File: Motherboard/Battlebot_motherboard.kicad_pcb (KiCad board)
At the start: 2 copper layers, 42 x 61.5 mm, 52 parts, among them J1 Reciever, J2 12Vin, J3 Fan connector, J4 BEC, J5 Conn_01x02_Socket, J6 Conn_01x02_Socket, U1 XIAO-RP2040-SMD, U2 L9958SBTR, U3 L9958SBTR

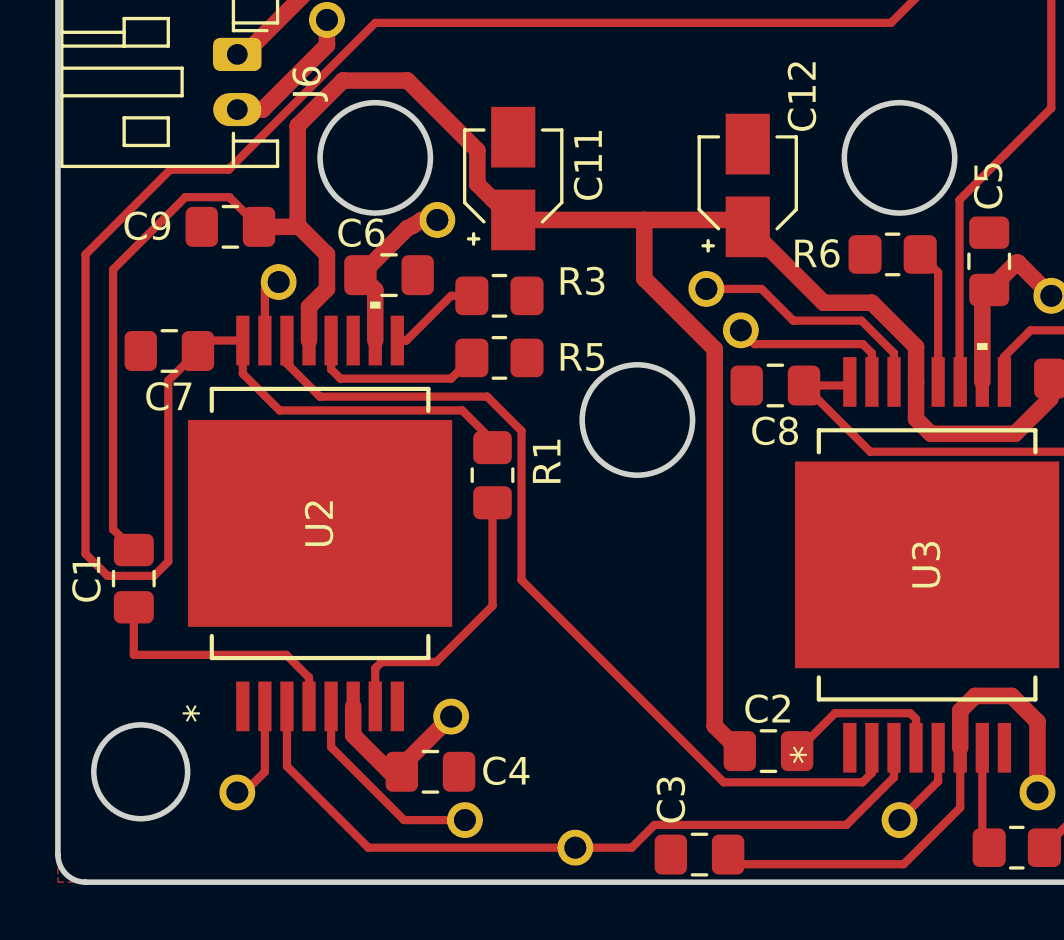
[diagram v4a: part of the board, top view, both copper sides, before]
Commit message: connected more of the ground pours
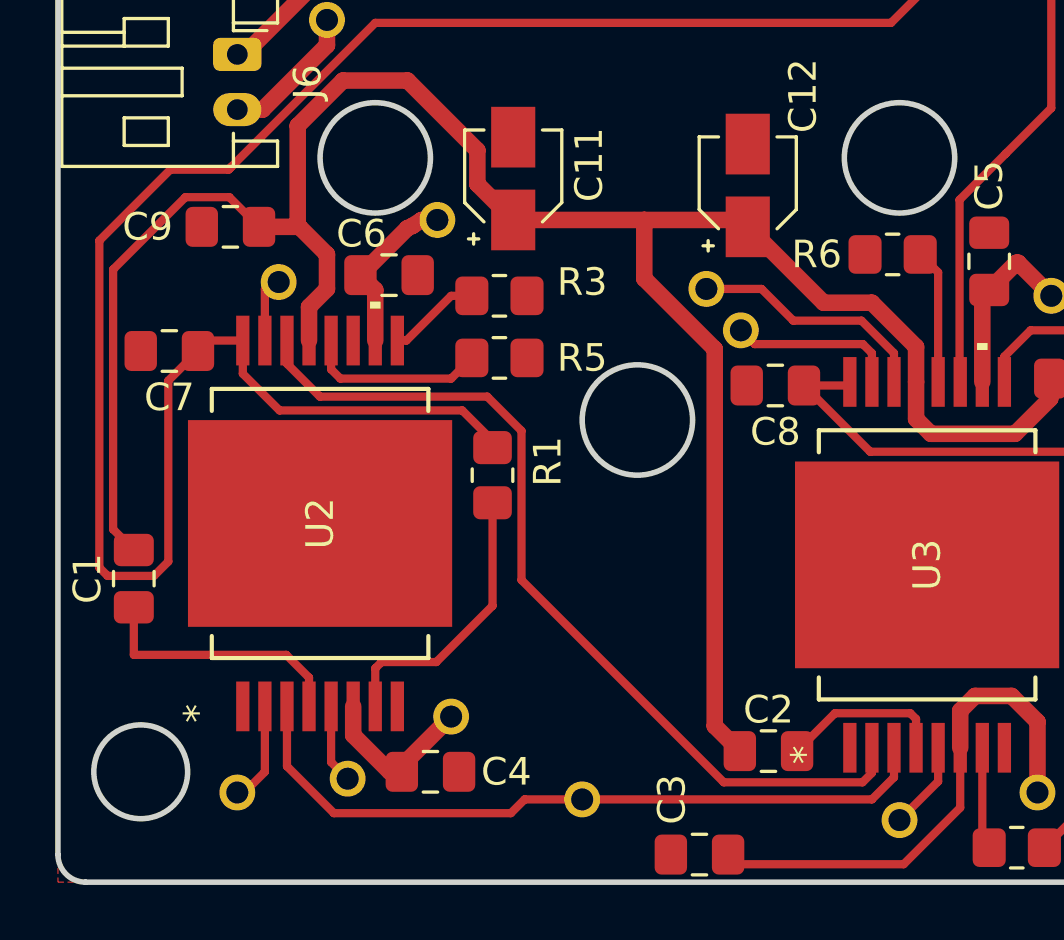
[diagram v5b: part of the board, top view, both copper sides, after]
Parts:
- moved ? 4.51 mm to (158.5, 99.2)
- moved ? 1.77 mm to (167.0, 100.0)
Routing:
- net DIR2: track 32.1 -> 27.5 mm
- net CS: track 31.2 -> 30.2 mm
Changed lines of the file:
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@@
 	(footprint ""
 		(layer "F.Cu")
-		(at 162.75 100.75)
+		(at 158.5 99.25)
 		(property "Reference" ""
 			(at 0 0 0)
@@
 	(footprint ""
 		(layer "F.Cu")
-		(at 166.75 101.75)
+		(at 167 100)
 		(property "Reference" ""
 			(at 0 0 0)
@@
 	)
 	(segment
-		(start 149 80.25)
-		(end 152.071315 77.178685)
-		(width 0.3)
-		(layer "F.Cu")
-		(net 8)
-	)
-	(segment
-		(start 152 91.380456)
-		(end 151.480456 91.9)
-		(width 0.3)
-		(layer "F.Cu")
-		(net 8)
-	)
-	(segment
 		(start 156.03085 85.9035)
 		(end 154.69965 84.5723)
@@
 	)
 	(segment
+		(start 149.5 91.6)
+		(end 149.5 79.75)
+		(width 0.3)
+		(layer "F.Cu")
+		(net 8)
+	)
+	(segment
+		(start 149.5 79.75)
+		(end 152.071315 77.178685)
+		(width 0.3)
+		(layer "F.Cu")
+		(net 8)
+	)
+	(segment
+		(start 153.075 83.75)
+		(end 152 84.825)
+		(width 0.3)
+		(layer "F.Cu")
+		(net 8)
+	)
+	(segment
 		(start 156.797 54.703)
 		(end 156.25 55.25)
@@
 	)
 	(segment
-		(start 184.6379 87.4035)
-		(end 184.6379 88)
+		(start 152 91.380456)
+		(end 151.480456 91.9)
 		(width 0.3)
 		(layer "F.Cu")
@@
 	)
 	(segment
-		(start 154.69965 83.3706)
-		(end 153.4544 83.3706)
+		(start 184.6379 87.4035)
+		(end 184.6379 88)
 		(width 0.3)
 		(layer "F.Cu")
@@
 	)
 	(segment
-		(start 152.071315 77.178685)
-		(end 154.178685 77.178685)
+		(start 154.69965 83.3706)
+		(end 153.4544 83.3706)
 		(width 0.3)
 		(layer "F.Cu")
@@
 	)
 	(segment
-		(start 151.480456 91.9)
-		(end 149.8 91.9)
-		(width 0.3)
-		(layer "F.Cu")
-		(net 8)
-	)
-	(segment
 		(start 154.69965 84.5723)
 		(end 154.69965 83.3706)
@@
 	)
 	(segment
-		(start 156.75 43)
-		(end 156.75 44.96)
+		(start 151.480456 91.9)
+		(end 149.8 91.9)
 		(width 0.3)
 		(layer "F.Cu")
@@
 	)
 	(segment
-		(start 189.35 83.2879)
-		(end 189.35 45.6)
+		(start 149.8 91.9)
+		(end 149.5 91.6)
 		(width 0.3)
 		(layer "F.Cu")
@@
 	)
 	(segment
-		(start 154.178685 77.178685)
-		(end 159.5 71.857371)
+		(start 156.75 43)
+		(end 156.75 44.96)
 		(width 0.3)
 		(layer "F.Cu")
@@
 	)
 	(segment
-		(start 153.075 83.75)
-		(end 152 84.825)
+		(start 189.35 83.2879)
+		(end 189.35 45.6)
 		(width 0.3)
 		(layer "F.Cu")
@@
 	)
 	(segment
-		(start 184.6379 88)
-		(end 184.6379 100.8621)
+		(start 154.178685 77.178685)
+		(end 159.5 71.857371)
 		(width 0.3)
 		(layer "F.Cu")
@@
 	)
 	(segment
-		(start 156.75 44.96)
-		(end 158.5 46.71)
+		(start 184.6379 88)
+		(end 184.6379 100.8621)
 		(width 0.3)
 		(layer "F.Cu")
@@
 	)
 	(segment
-		(start 149 91.1)
-		(end 149 80.25)
+		(start 156.75 44.96)
+		(end 158.5 46.71)
 		(width 0.3)
 		(layer "F.Cu")
@@
 	)
 	(segment
-		(start 178.192629 71.857371)
-		(end 182.05 68)
+		(start 152.071315 77.178685)
+		(end 154.178685 77.178685)
 		(width 0.3)
 		(layer "F.Cu")
@@
 	)
 	(segment
-		(start 157 42.75)
-		(end 156.75 43)
+		(start 152 84.825)
+		(end 152 91.380456)
 		(width 0.3)
 		(layer "F.Cu")
@@
 	)
 	(segment
-		(start 152 84.825)
-		(end 152 91.380456)
+		(start 178.192629 71.857371)
+		(end 182.05 68)
 		(width 0.3)
 		(layer "F.Cu")
@@
 	)
 	(segment
-		(start 149.8 91.9)
-		(end 149 91.1)
+		(start 157 42.75)
+		(end 156.75 43)
 		(width 0.3)
 		(layer "F.Cu")
@@
 	)
 	(segment
+		(start 157.90005 98.65005)
+		(end 158.5 99.25)
+		(width 0.3)
+		(layer "F.Cu")
+		(net 17)
+	)
+	(segment
 		(start 166.4756 46.301)
 		(end 166.4756 47.676)
@@
 	(segment
 		(start 157.90005 96.6294)
-		(end 157.90005 98.105506)
-		(width 0.3)
-		(layer "F.Cu")
-		(net 17)
-	)
-	(segment
-		(start 160.544544 100.75)
-		(end 162.75 100.75)
-		(width 0.3)
-		(layer "F.Cu")
-		(net 17)
-	)
-	(segment
-		(start 157.90005 98.105506)
-		(end 160.544544 100.75)
+		(end 157.90005 98.65005)
 		(width 0.3)
 		(layer "F.Cu")
@@
 	)
 	(segment
-		(start 168.794544 101.75)
-		(end 169.619544 100.925)
+		(start 164.914214 100)
+		(end 177.5 100)
 		(width 0.3)
 		(layer "F.Cu")
@@
 	)
 	(segment
-		(start 178.29985 99.20015)
-		(end 178.29985 98.1294)
+		(start 164.414214 100.5)
+		(end 164.914214 100)
 		(width 0.3)
 		(layer "F.Cu")
@@
 	)
 	(segment
-		(start 159.25 101.75)
-		(end 168.794544 101.75)
+		(start 156.29985 96.6294)
+		(end 156.29985 98.79985)
 		(width 0.3)
 		(layer "F.Cu")
@@
 	)
 	(segment
-		(start 163.9356 64.8144)
-		(end 163 65.75)
+		(start 178.29985 99.20015)
+		(end 178.29985 98.1294)
 		(width 0.3)
 		(layer "F.Cu")
@@
 	)
 	(segment
-		(start 176.575 100.925)
-		(end 178.29985 99.20015)
+		(start 163.9356 64.8144)
+		(end 163 65.75)
 		(width 0.3)
 		(layer "F.Cu")
@@
 	)
 	(segment
-		(start 156.29985 96.6294)
-		(end 156.29985 98.79985)
+		(start 156.29985 98.79985)
+		(end 158 100.5)
 		(width 0.3)
 		(layer "F.Cu")
@@
 	)
 	(segment
-		(start 169.619544 100.925)
-		(end 176.575 100.925)
+		(start 158 100.5)
+		(end 164.414214 100.5)
 		(width 0.3)
 		(layer "F.Cu")
@@
 	)
 	(segment
-		(start 156.29985 98.79985)
-		(end 159.25 101.75)
+		(start 163.9356 62.466)
+		(end 163.9356 64.8144)
 		(width 0.3)
 		(layer "F.Cu")
@@
 	)
 	(segment
-		(start 163.9356 62.466)
-		(end 163.9356 64.8144)
+		(start 177.5 100)
+		(end 178.29985 99.20015)
 		(width 0.3)
 		(layer "F.Cu")

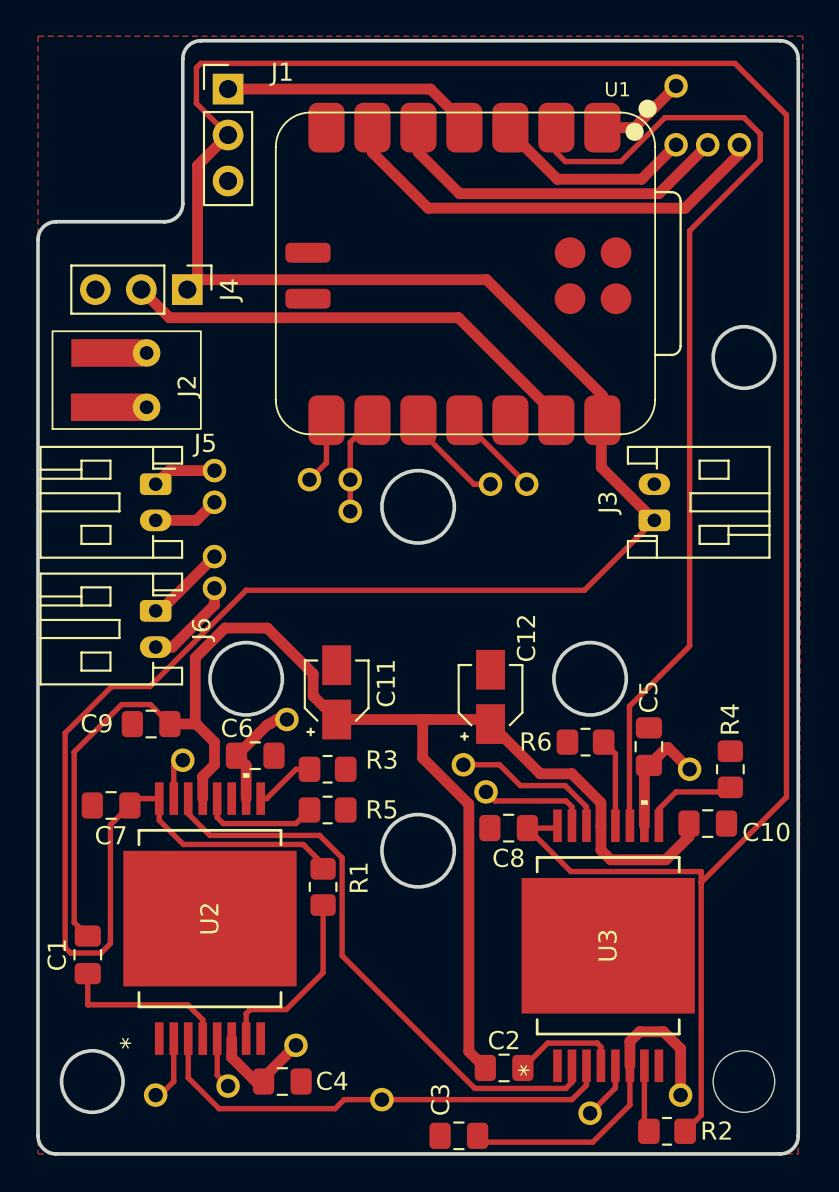
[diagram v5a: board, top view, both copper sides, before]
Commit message: reroute using 2 layers and fix 1 connector
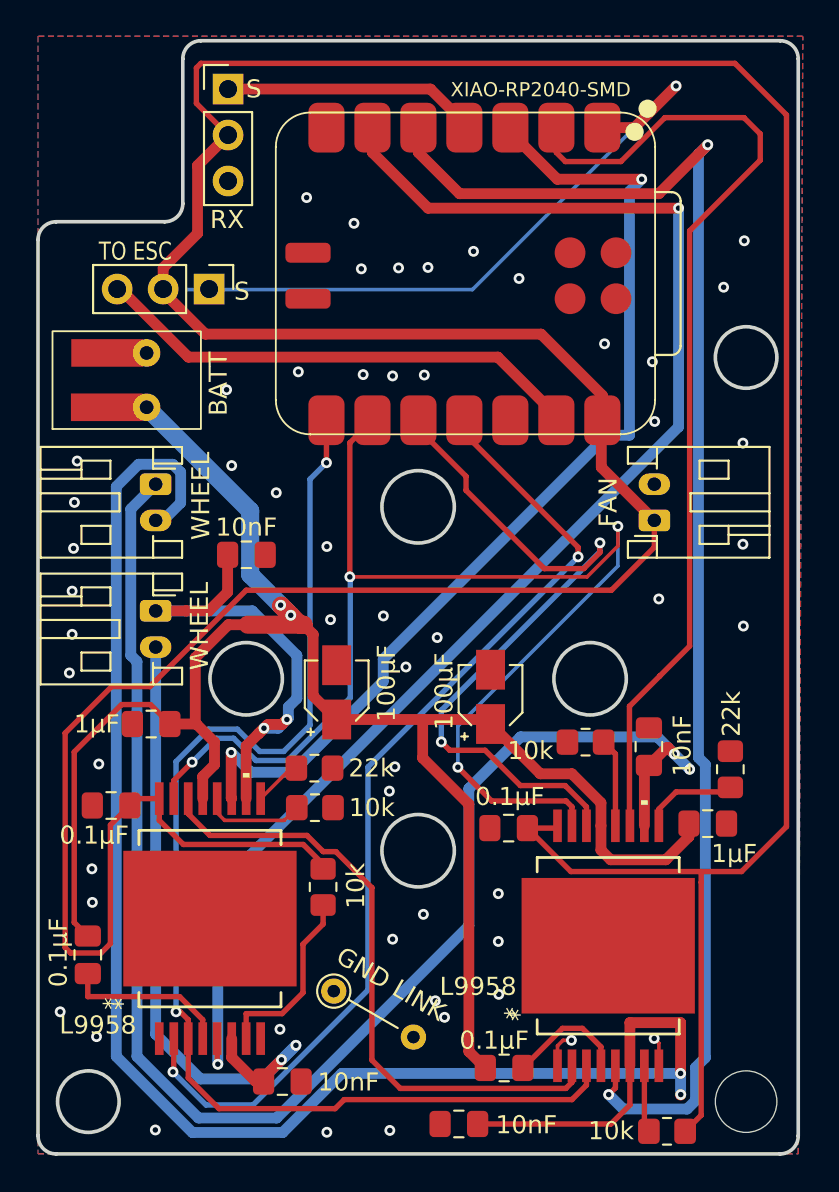
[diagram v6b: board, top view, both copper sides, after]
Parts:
- removed ? (x23): , 
- removed the REF** at (186.8, 47.2)
- added GND LINK: 0, Resistor_THT:R_Axial_DIN0204_L3.6mm_D1.6mm_P5.08mm_Vertical, F.Cu at (164.3, 94.0)
- TO ESC: renamed from J4
- moved 10nF 11.1 mm to (159.5, 69.9)
- moved TO ESC 1.20 mm to (157.5, 55.2)
- moved 22k 0.73 mm to (163.3, 81.7)
- moved 10k 0.72 mm to (163.3, 83.9)
- moved 10nF 0.65 mm to (171.2, 101.3)
- renumbered C2 to 0.1µF, C7 to 0.1µF, C8 to 0.1µF, C1 to 0.1µF, C11 to 100µF, C12 to 100µF, R5 to 10k, R1 to 10k, R6 to 10k, R2 to 10k, C4 to 10nF, C5 to 10nF, C6 to 10nF, C3 to 10nF, C9 to 1µF, C10 to 1µF, R3 to 22k, R4 to 22k, J2 to BATT, J3 to FAN, U2 to L9958, U3 to L9958, J1 to RX, J6 to WHEEL, J5 to WHEEL, U1 to XIAO-RP2040-SMD
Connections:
- TO ESC pad 1: +5V -> PWM3
- TO ESC pad 2: Net-(J4-Pin_2) -> +5V
- TO ESC pad 3: PWM3 -> Net-(J4-Pin_3)
- XIAO-RP2040-SMD pad 13: Net-(J4-Pin_2) -> Net-(J4-Pin_3)
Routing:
- net Net-(J5-Pin_1): track 10.2 -> 83.6 mm, vias 0 -> 2
- net Net-(J5-Pin_2): track 22.6 -> 93.7 mm, vias 0 -> 2
- net SCK: track 13.9 -> 71.4 mm, vias 0 -> 4
- net DIR1: track 23.0 -> 79.9 mm, vias 0 -> 2
- net DIR2: track 27.5 -> 78.8 mm, vias 0 -> 2
- net µSI: track 8.39 -> 55.0 mm, vias 0 -> 2
- net PWM2: track 11.3 -> 56.5 mm, vias 0 -> 2
- net CS: track 30.2 -> 68.7 mm, vias 0 -> 2
- net PWM3: track 5.03 -> 36.7 mm, vias 0 -> 1
- net Net-(J4-Pin_3): track 0.00 -> 27.2 mm
- net Net-(J4-Pin_2): track 26.1 -> 0.00 mm
- net Net-(J6-Pin_2): track 11.2 -> 37.0 mm, vias 0 -> 2
- net µSO: track 14.5 -> 40.2 mm, vias 0 -> 2
- net +12V: track 85.7 -> 103.6 mm, vias 0 -> 2
- net Net-(J6-Pin_1): track 10.7 -> 26.7 mm, vias 0 -> 2
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- added copper zone on B.Cu, net GND
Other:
- outline, holes or cut-outs redrawn
- board text added: "S"

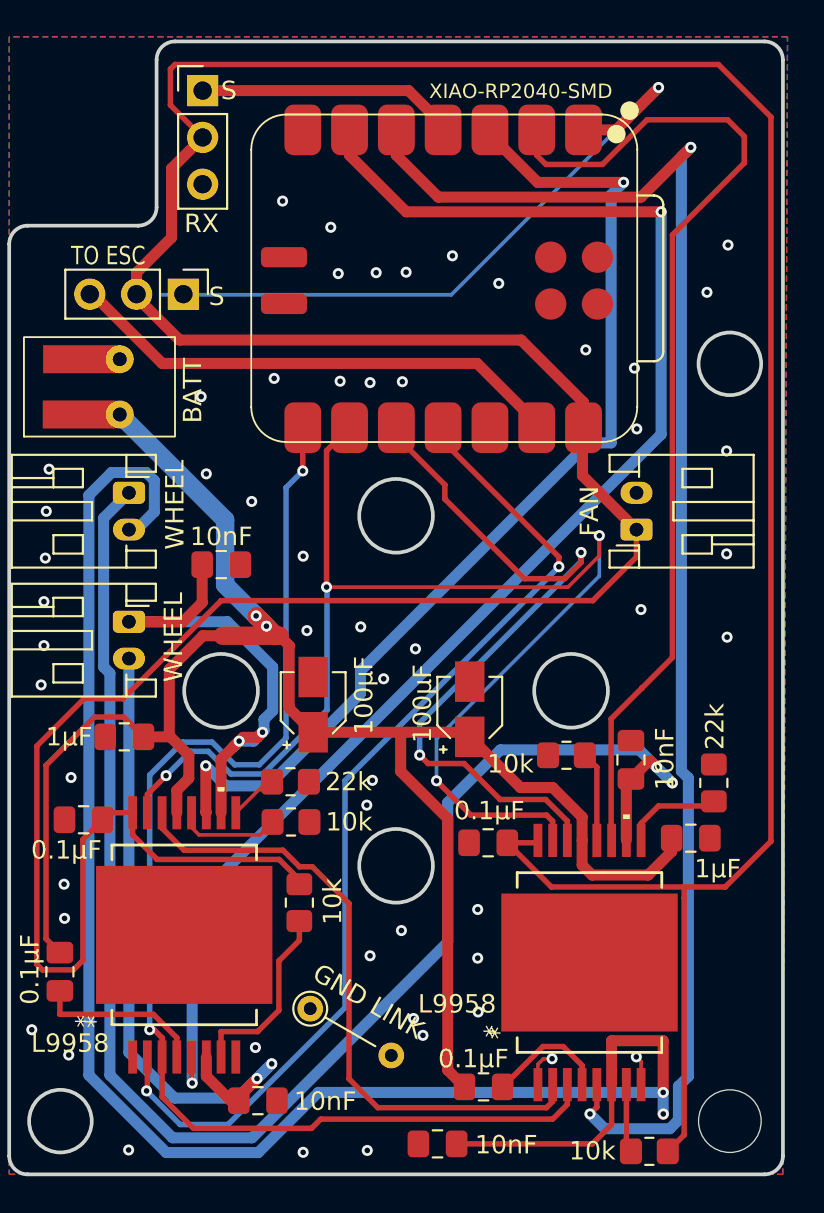
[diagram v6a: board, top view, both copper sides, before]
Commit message: cleaned routing a little bit and updated silkscreen
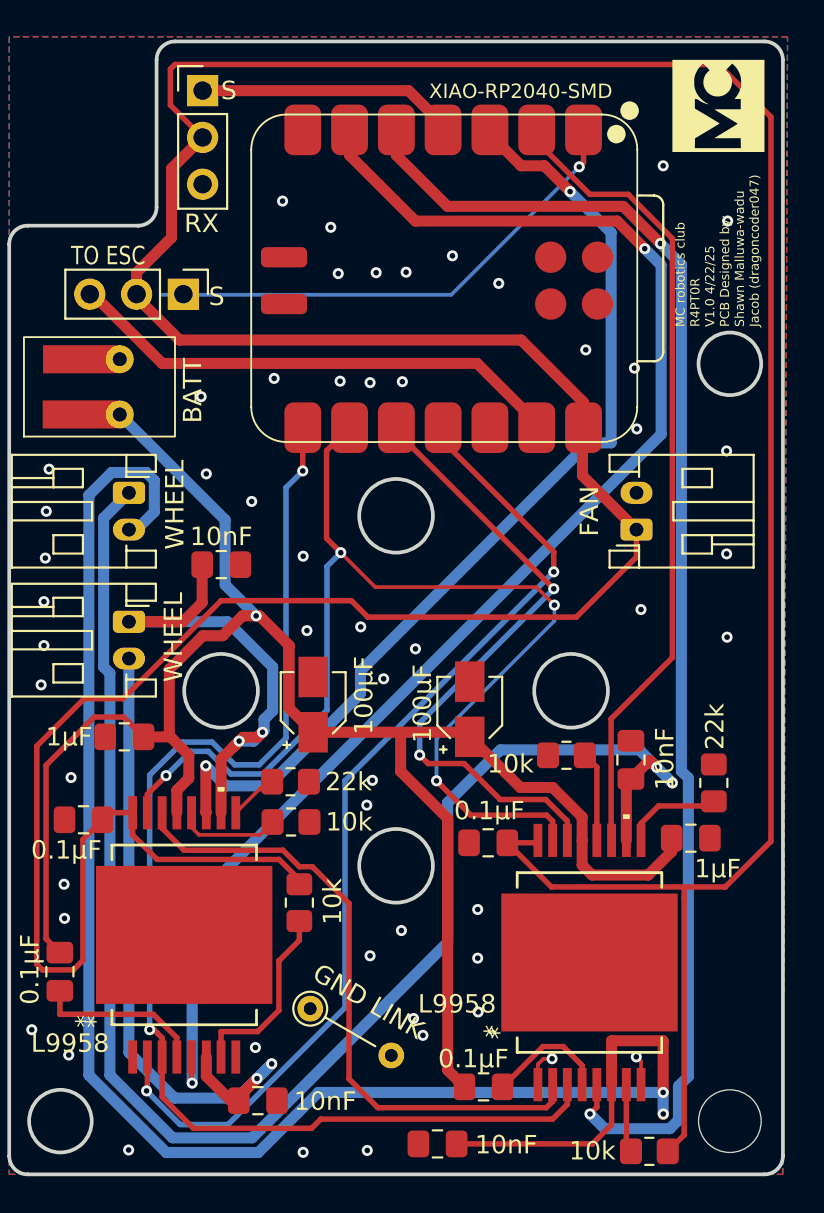
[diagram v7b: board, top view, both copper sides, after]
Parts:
- added G***: LOGO, LOGO, F.Cu at (186.5, 45.0)
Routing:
- net PWM1: track 55.4 -> 44.2 mm
- net PWM3: track 36.7 -> 27.7 mm
- net SCK: track 71.4 -> 63.4 mm
- net DIR1: track 79.9 -> 73.2 mm
- net µSO: track 40.2 -> 34.9 mm
- net PWM2: track 56.5 -> 53.9 mm
- net DIR2: track 78.8 -> 77.1 mm
- net +12V: track 103.6 -> 102.0 mm, vias 2 -> 1
- net +5V: track 230.1 -> 230.9 mm
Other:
- board text added: "MC robotics club R4PT0R V1.0 4/22/25 PCB Designed by: Shawn Malluwa-wadu Jacob (dragoncoder047)"

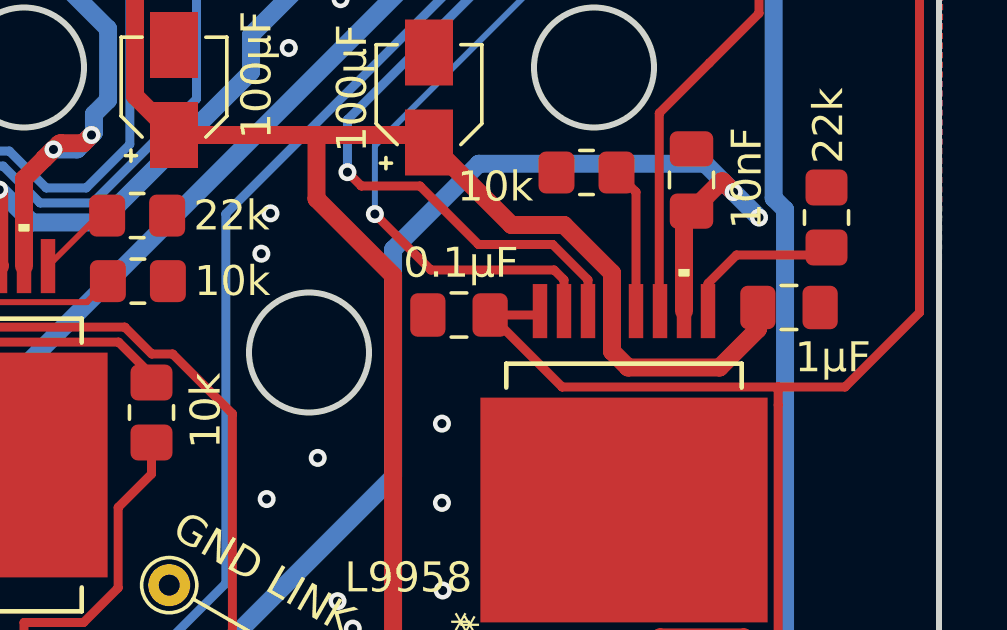
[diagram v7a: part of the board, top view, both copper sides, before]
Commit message: fixed ground plane with another via
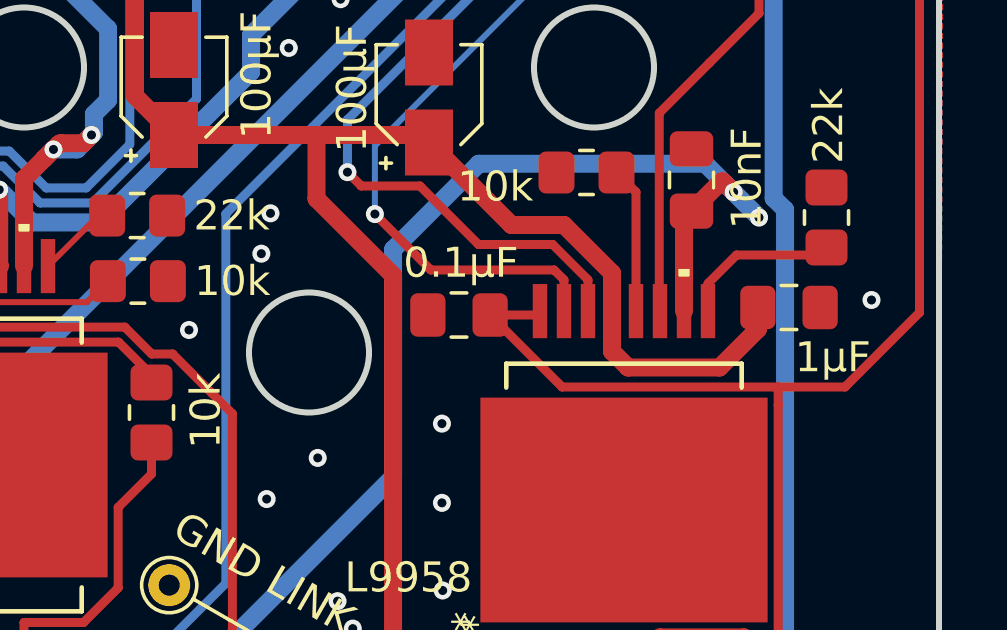
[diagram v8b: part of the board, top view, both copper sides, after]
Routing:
- net GND: vias 54 -> 56
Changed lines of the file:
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@@
+	)
+	(via
+		(at 165 85.5)
+		(size 0.6)
+		(drill 0.3)
+		(layers "F.Cu" "B.Cu")
+		(free yes)
+		(net 3)
 	)
 	(via
@@
 		(size 0.6)
 		(drill 0.3)
+		(layers "F.Cu" "B.Cu")
+		(free yes)
+		(net 3)
+	)
+	(via
+		(at 187.75 84.5)
+		(size 0.6)
+		(drill 0.3)
